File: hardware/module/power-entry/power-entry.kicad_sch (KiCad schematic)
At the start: 19 parts

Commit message: WIP module schematics: footprints, bought-part fields, and the two board projects (module-main, module-jack)
Recovered from a container restart; not yet exported or checked.

Co-Authored-By: Claude Opus 5.5 <noreply@anthropic.com>
Claude-Session: https://claude.ai/code/session_01LmB4muFXnoLprWX4JzuJ5A
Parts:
- C-DEC-REG-IN: footprint (none) -> Capacitor_SMD:C_0805_2012Metric; Assembly (none) -> machine; LCSC (none) -> C49678; MPN (none) -> CC0805KRX7R9BB104; Manufacturer (none) -> YAGEO
- C-REG-ADJ: footprint (none) -> Capacitor_SMD:C_0805_2012Metric; Assembly (none) -> machine; LCSC (none) -> C15850; MPN (none) -> CL21A106KAYNNNE; Manufacturer (none) -> Samsung Electro-Mechanics
- C-REG-OUT: footprint (none) -> Capacitor_SMD:C_0805_2012Metric; Assembly (none) -> machine; LCSC (none) -> C28323; MPN (none) -> CL21B105KBFNNNE; Manufacturer (none) -> Samsung Electro-Mechanics
- C1: footprint (none) -> Capacitor_THT:CP_Radial_D6.3mm_P2.50mm; Assembly (none) -> hand; LCSC (none) -> C165558; MPN (none) -> NXA25V100M6.3*11 2.5TP; Manufacturer (none) -> SamYoung
- C2, C3, C4: footprint (none) -> Capacitor_THT:CP_Radial_D5.0mm_P2.00mm; Assembly (none) -> hand; LCSC (none) -> C371230; MPN (none) -> NXB25V47M5*11 2.5TP; Manufacturer (none) -> SamYoung
- D1, D2, D3: footprint (none) -> Diode_THT:D_DO-41_SOD81_P10.16mm_Horizontal; Assembly (none) -> hand; LCSC (none) -> C507852; MPN (none) -> 1N5817-T; Manufacturer (none) -> Diodes Incorporated
- FB1, FB2, FB3, FB4: footprint (none) -> Inductor_SMD:L_1206_3216Metric; Assembly (none) -> machine; LCSC (none) -> C2441375; MPN (none) -> MI1206K601R-10; Manufacturer (none) -> Laird
- J-PWR-EURO: footprint (none) -> Connector_IDC:IDC-Header_2x08_P2.54mm_Vertical; Assembly (none) -> hand; LCSC (none) -> C492443; MPN (none) -> BH254V-16P; Manufacturer (none) -> XFCN
- NT-AGND-MOD: footprint (none) -> NetTie:NetTie-2_SMD_Pad0.5mm; Assembly (none) -> none
- R-REG-SET-HI: footprint (none) -> Resistor_SMD:R_0805_2012Metric; Assembly (none) -> machine; LCSC (none) -> C50670161; MPN (none) -> TC0525B4750T5G; Manufacturer (none) -> UNI-ROYAL(Uniroyal Elec)
- R-REG-SET-LO: footprint (none) -> Resistor_SMD:R_0805_2012Metric; Assembly (none) -> machine; LCSC (none) -> C513734; MPN (none) -> RT0805BRD07150RL; Manufacturer (none) -> YAGEO
- U-REG-DAC: footprint (none) -> Package_TO_SOT_THT:TO-92_Inline; Assembly (none) -> hand; LCSC (none) -> C5267874; MPN (none) -> LM317LZ; Manufacturer (none) -> STMicroelectronics

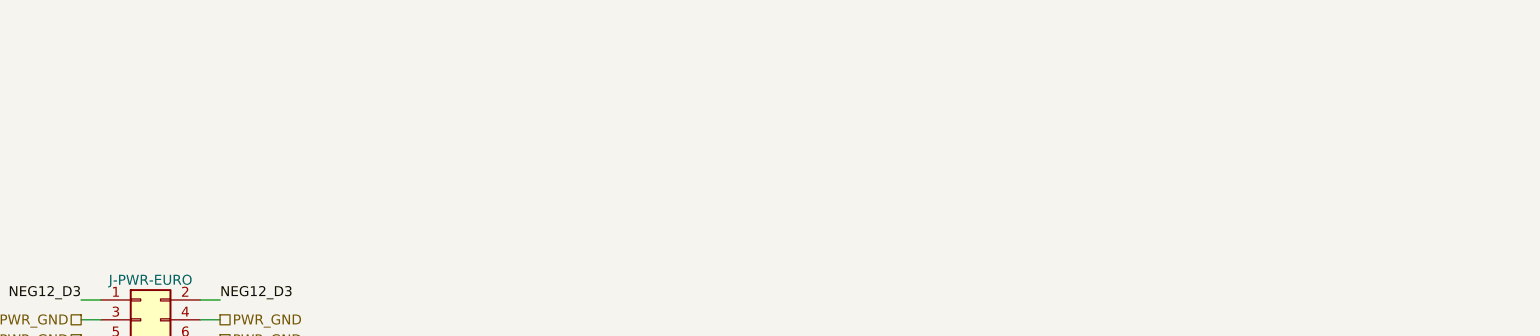
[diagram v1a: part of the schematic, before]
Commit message: Module schematics: the ten circuits' netlists exported from their sheets; J-B2B-MOD allocated by position
- Every module circuit's netlist.yaml is now EXPORTED from its KiCad sheet
  (ADR 0019), identical part by part and net by net to the hand-written one,
  including its foreign: parts. kicad.py exports foreign: from FOREIGN lines of
  sheet text; without it the breath receive page's R1 went unresolved.
- J-B2B-MOD, re-allocated: the pots' nets on the top rows (the pots sit above
  the header), each side's pot and jacks in its own column, a ground on the
  diagonal of every other row so every signal but the LED's +12 V has a ground
  pin beside it.
- kicad.py check: J-B2B-MOD is one conductor per pin on both module boards, and
  the main board's etherCON matches hardware/interfaces/spi-link pin for pin.
- sch.py: a board's sub-sheet pin with one member is a no-connect again (the
  interfaces' spare-label rule assumed a part pin).

Co-Authored-By: Claude Opus 5.5 <noreply@anthropic.com>
Claude-Session: https://claude.ai/code/session_01LmB4muFXnoLprWX4JzuJ5A
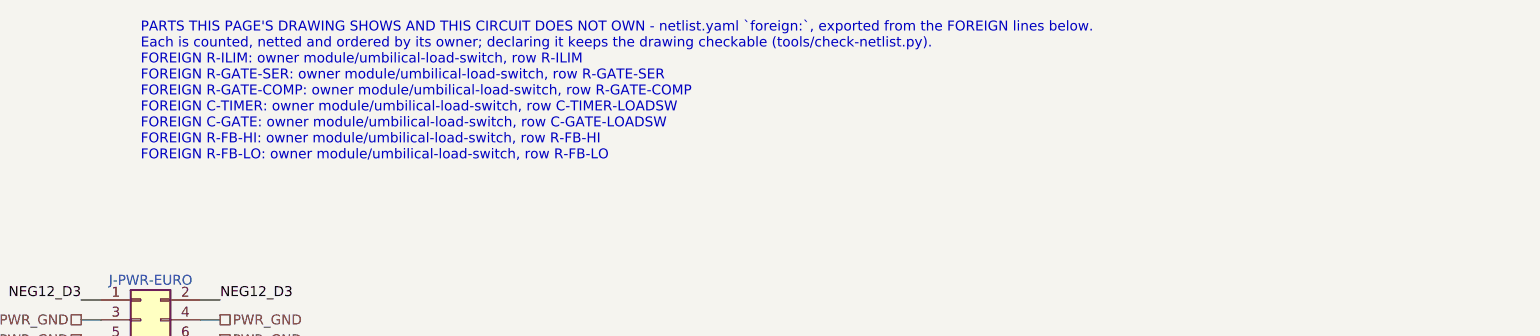
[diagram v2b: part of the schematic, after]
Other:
- note added: "PARTS THIS PAGE'S DRAWING SHOWS AND THIS CIRCUIT DOES NOT OWN - netlist.yaml `foreign:`, exported from the FOREIGN lines below. Each is counted, netted and ordered by its owner; declaring it keeps the drawing checkable (tools/check-netlist.py). FOREIGN R-ILIM: owner module/umbilical-load-switch, row R-ILIM FOREIGN R-GATE-SER: owner module/umbilical-load-switch, row R-GATE-SER FOREIGN R-GATE-COMP: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"
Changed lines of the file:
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@@
   (no_connect (at 48.26 71.12))
   (text "FROM THE HAND-WRITTEN NETLIST THIS SHEET REPLACES (verbatim; the part notes are on each part's Note field):\n\nAUTHORITATIVE for connectivity. The drawing in power-entry.md is a representation of this file.\n\nSCOPE. That drawing shows the whole load switch - LT1641, R-ILIM, the timer and gate capacitors, the FB\ndivider and Q-LOADSW - so the export path can be read in one place. THOSE ARE module/umbilical-load-switch's\nPARTS and are declared `foreign:` here. This circuit owns the rail entry, the four bead-and-bulk branches and\nthe LM317.\n\n[J-PWR-EURO] THE HEADER'S SIXTEEN PINS, as the Doepfer bus numbers them: -12 V on the pair at pin 1 (the\nribbon's red stripe), GND on three pairs, +12 V, +5 V, then the bus CV and Gate, which this module does not\nuse [ds mechanical/DOEPFER-A100-BUS-CONNECTORS-a100b_e.gif]. Each supply is carried on both pins of its pair;\nCV and Gate are no-connects by decision.\n\n[of] qty 3: D1, D2, D3\n\n[of] qty 4: FB1..FB4\n\n[of] qty 4: C1..C4\n\n[NT-AGND-MOD] THE ANALOG STAR'S TIE. \"One origin, at the IDC's ground pin ... The analog return is its own\nregion joining at the star\" (power-entry.md, Grounding). A net tie is how a board joins two named nets at one\nplace and nowhere else, as NT-AGND does on the instrument's carrier. DIG_GND HAS NO TIE HERE: where it meets\nthe others is dig-gnd-topology, which is disputed.\n\n[PWR_EXPORT] The D2 branch. WHERE IT TERMINATES IS NOT DECIDABLE FROM THE DRAWING and is deliberately not\nasserted here - see the note at the foot of this file.\n\n[CV_13] The bus CV and Gate: a no-connect each, by decision.\n\nOPEN, AND NOT GUESSED AT.\n\n`BUS_POS12_RAW` is taken BEFORE D1/D2. Both Interfaces tables say so in the same words - power-entry.md:31\n\"The branch is taken **before** the diodes\" and umbilical-load-switch.md:18 \"Taken before the...\" - so two\nindependent statements agree and this file follows them.\n\nTHE DRAWING CANNOT BE READ THAT WAY WITH CONFIDENCE. It shows the D2 branch running into the load-switch\nblock, and the left-hand spine is the connector body rather than a rail, so the two readings are not\ndistinguishable from the ASCII. That is the whole argument for this file existing: A PICTURE CAN BE AMBIGUOUS\nAND A NETLIST CANNOT.\n\nSo the D2 branch's far end is left unasserted. It is one of: - the exported rail's reverse protection, with\nthe load switch upstream on the raw bus, which is what both tables describe; or - in series with the load\nswitch output, which is what the drawing looks like and which would give the exported rail protection the\ntables do not credit it with. The difference is what reverse-polarity protection the instrument actually has.\nResolve it on the page, then state it here - do not resolve it here from a reading of the picture.\n\nThe load switch's own parts (R-ILIM, the timer and gate network, the FB divider) are `foreign:` above so the\ndrawing checks, and are NOT netted here: a part belongs to one circuit's netlist, or two files can disagree\nabout one connection and both look right." (at 408.94 38.099999999999994 0) (effects (font (size 1.27 1.27)) (justify left top)))
+  (text "PARTS THIS PAGE'S DRAWING SHOWS AND THIS CIRCUIT DOES NOT OWN - netlist.yaml `foreign:`, exported from the FOREIGN lines below.\nEach is counted, netted and ordered by its owner; declaring it keeps the drawing checkable (tools/check-netlist.py).\nFOREIGN R-ILIM: owner module/umbilical-load-switch, row R-ILIM\nFOREIGN R-GATE-SER: owner module/umbilical-load-switch, row R-GATE-SER\nFOREIGN R-GATE-COMP: owner module/umbilical-load-switch, row R-GATE-COMP\nFOREIGN C-TIMER: owner module/umbilical-load-switch, row C-TIMER-LOADSW\nFOREIGN C-GATE: owner module/umbilical-load-switch, row C-GATE-LOADSW\nFOREIGN R-FB-HI: owner module/umbilical-load-switch, row R-FB-HI\nFOREIGN R-FB-LO: owner module/umbilical-load-switch, row R-FB-LO" (at 40.64 17.78 0) (effects (font (size 1.27 1.27)) (justify left top)))
   (sheet_instances (path "/" (page "1")))
 )

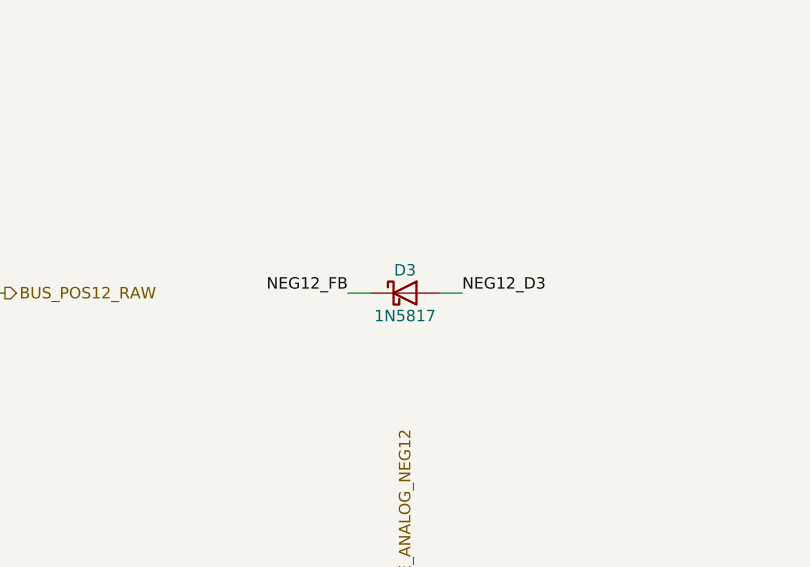
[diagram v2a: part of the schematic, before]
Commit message: Module: D3 turned round; pitch trims made buildable and bipolar; LT5400 pad and order code; breath-zero range resistor
D3 (the -12 V entry diode) was netlisted anode-to-bus, reverse-biased in
normal running (found by the analog sims): cathode to the bus now.
TRIM-OFFSET spans VREFOUT-AGND and injects through R-VREF-INJ against
R-VREF-SER into the follower at gain 1.02 (R-VREF-FB/R-VREF-GND): 2.500 V at
mid-travel, -60/+50 mV. It also holds the 3-state VREFOUT at 0 V while the
DAC's reference is disabled. TRIM-GAIN is centred by R-GAIN-CTR in the R1 leg
(+/-1 %) and its CW end strapped to the wiper. RN-PITCH carries its exposed
pad as pin 9 to AGND_MOD, spares tied down; ordered LT5400BIMS8E-1#PBF.
R-OPAMP-IN is six; R-TRIM-RANGE split into real parts. R-ZERO-TOP gives
TRIM-BREATH-ZERO the 0-1.0 V range its page specifies. Page text follows.

Co-Authored-By: Claude Opus 5.5 <noreply@anthropic.com>
Claude-Session: https://claude.ai/code/session_01LmB4muFXnoLprWX4JzuJ5A
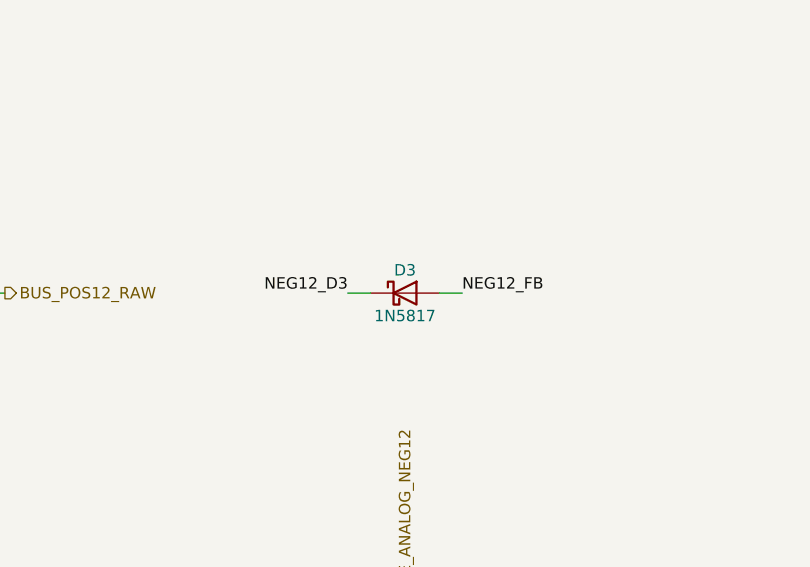
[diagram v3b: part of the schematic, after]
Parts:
- D3: Note Reverse protection, -12 V branch -> Reverse protection, -12 V branch. CATHODE TO THE BUS, anode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
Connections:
- net NEG12_D3: now also D3.1 (K); no longer D3.2 (A)
- net NEG12_FB: now also D3.2 (A); no longer D3.1 (K)
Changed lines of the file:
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@@
     (property "Pins" "A=2(A) K=1(K)" (at 142.24 142.24 0) (effects (font (size 1.27 1.27)) hide))
     (property "Drawn_as" "D3" (at 142.24 142.24 0) (effects (font (size 1.27 1.27)) hide))
-    (property "Note" "Reverse protection, -12 V branch" (at 142.24 142.24 0) (effects (font (size 1.27 1.27)) hide))
+    (property "Note" "Reverse protection, -12 V branch. CATHODE TO THE BUS, anode to the module's -12 V rail: the rail's current flows out of the module into the bus's -12 V, so this is the one entry diode the other way round from D1/D2" (at 142.24 142.24 0) (effects (font (size 1.27 1.27)) hide))
     (property "Pins_source" "datasheets/discrete-and-power/1N5817.pdf: DO-41, cathode band; KiCad pin 1 cathode" (at 142.24 142.24 0) (effects (font (size 1.27 1.27)) hide))
     (property "Manufacturer" "Diodes Incorporated" (at 142.24 142.24 0) (effects (font (size 1.27 1.27)) hide))
@@
   (label "NEG12_D3" (at 50.8 53.34 0) (fields_autoplaced) (effects (font (size 1.27 1.27)) (justify left bottom)))
   (wire (pts (xy 146.05 142.24) (xy 148.59 142.24)) (stroke (width 0) (type default)))
-  (label "NEG12_D3" (at 148.59 142.24 0) (fields_autoplaced) (effects (font (size 1.27 1.27)) (justify left bottom)))
+  (label "NEG12_FB" (at 148.59 142.24 0) (fields_autoplaced) (effects (font (size 1.27 1.27)) (justify left bottom)))
   (wire (pts (xy 138.43 142.24) (xy 135.89 142.24)) (stroke (width 0) (type default)))
-  (label "NEG12_FB" (at 135.89 142.24 180) (fields_autoplaced) (effects (font (size 1.27 1.27)) (justify right bottom)))
+  (label "NEG12_D3" (at 135.89 142.24 180) (fields_autoplaced) (effects (font (size 1.27 1.27)) (justify right bottom)))
   (wire (pts (xy 294.64 138.43) (xy 294.64 135.89)) (stroke (width 0) (type default)))
   (label "NEG12_FB" (at 294.64 135.89 90) (fields_autoplaced) (effects (font (size 1.27 1.27)) (justify left bottom)))
